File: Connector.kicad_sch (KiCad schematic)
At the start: 3 parts, among them J7 Conn_02x10_Odd_Even

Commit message: Не битый репозиторий
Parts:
- J7: footprint Connector_PinSocket_2.54mm:PinSocket_2x10_P2.54mm_Vertical -> Connector_PinSocket_2.00mm:PinSocket_2x10_P2.00mm_Vertical
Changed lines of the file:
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@@
       (effects (font (size 1.27 1.27)) hide)
     )
-    (property "Footprint" "Connector_PinSocket_2.54mm:PinSocket_2x10_P2.54mm_Vertical" (at 156.21 83.82 0)
+    (property "Footprint" "Connector_PinSocket_2.00mm:PinSocket_2x10_P2.00mm_Vertical" (at 156.21 83.82 0)
       (effects (font (size 1.27 1.27)) hide)
     )

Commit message: Первый вариант
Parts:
- removed J7: Conn_02x10_Odd_Even, Connector_PinSocket_2.00mm:PinSocket_2x10_P2.00mm_Vertical, symbol Connector_Generic:Conn_02x10_Odd_Even
- added J10, J11, J12, J13, J14, J15, J7, J9: Conn_01x02_Pin, Connector_PinHeader_2.54mm:PinHeader_1x02_P2.54mm_Vertical_SMD_Pin1Left, symbol Connector:Conn_01x02_Pin
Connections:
- net +24V: now also J11.1 (Pin_1)
- net A: now also J10.1 (Pin_1)
- net B: now also J7.1 (Pin_1)
- net C: now also J15.2 (Pin_2)
- net G1: now also J10.2 (Pin_2)
- net G2: now also J9.2 (Pin_2)
- net G3: now also J7.2 (Pin_2)
- net G4: now also J13.1 (Pin_1)
- net G5: now also J15.1 (Pin_1)
- net G6: now also J14.1 (Pin_1)
- net GND: now also J11.2 (Pin_2), J13.2 (Pin_2), J14.2 (Pin_2), J9.1 (Pin_1)
- new net Shunt+: J12.2 (Pin_2)
- new net Shunt-: J12.1 (Pin_1)

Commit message: Сохранил схему
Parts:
- added J16: Conn_01x02_Pin, Connector_PinHeader_2.54mm:PinHeader_1x02_P2.54mm_Vertical_SMD_Pin1Left, symbol Connector:Conn_01x02_Pin
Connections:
- new net NTC+: J16.2 (Pin_2)
- new net NTC-: J16.1 (Pin_1)

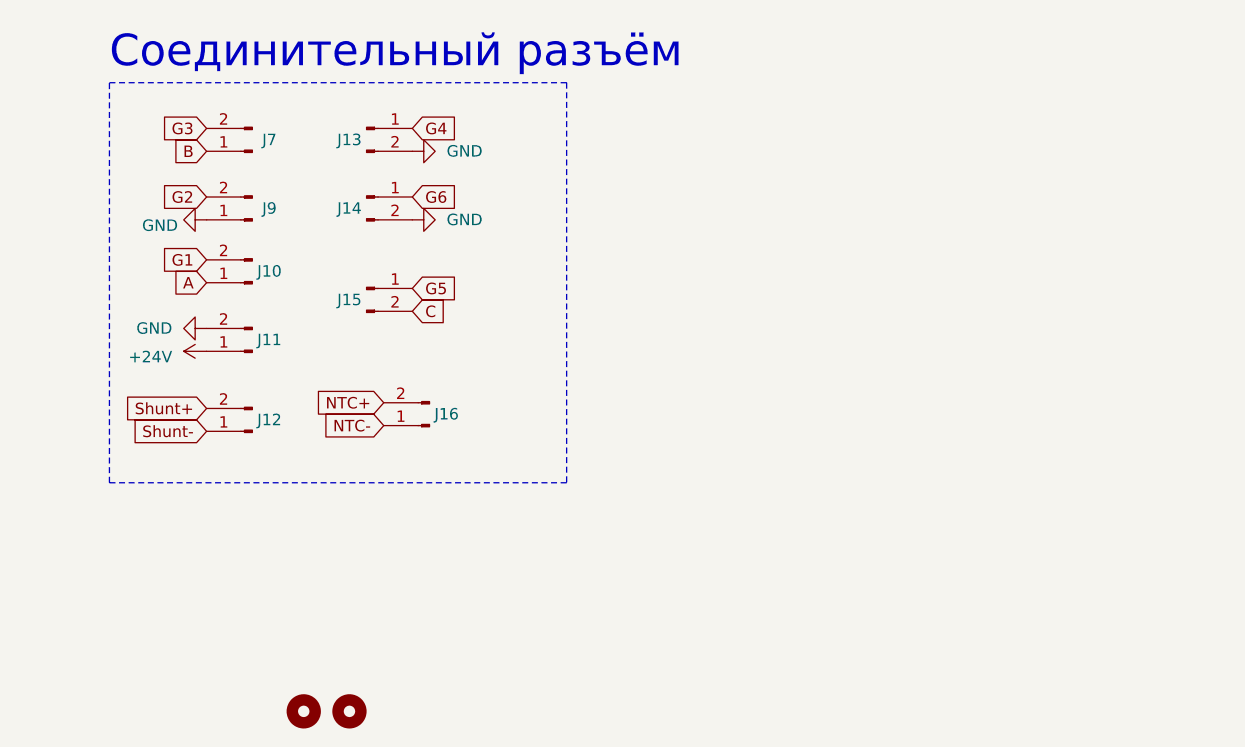
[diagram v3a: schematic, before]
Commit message: Заменил разъёмы 2.54 на 1.27мм
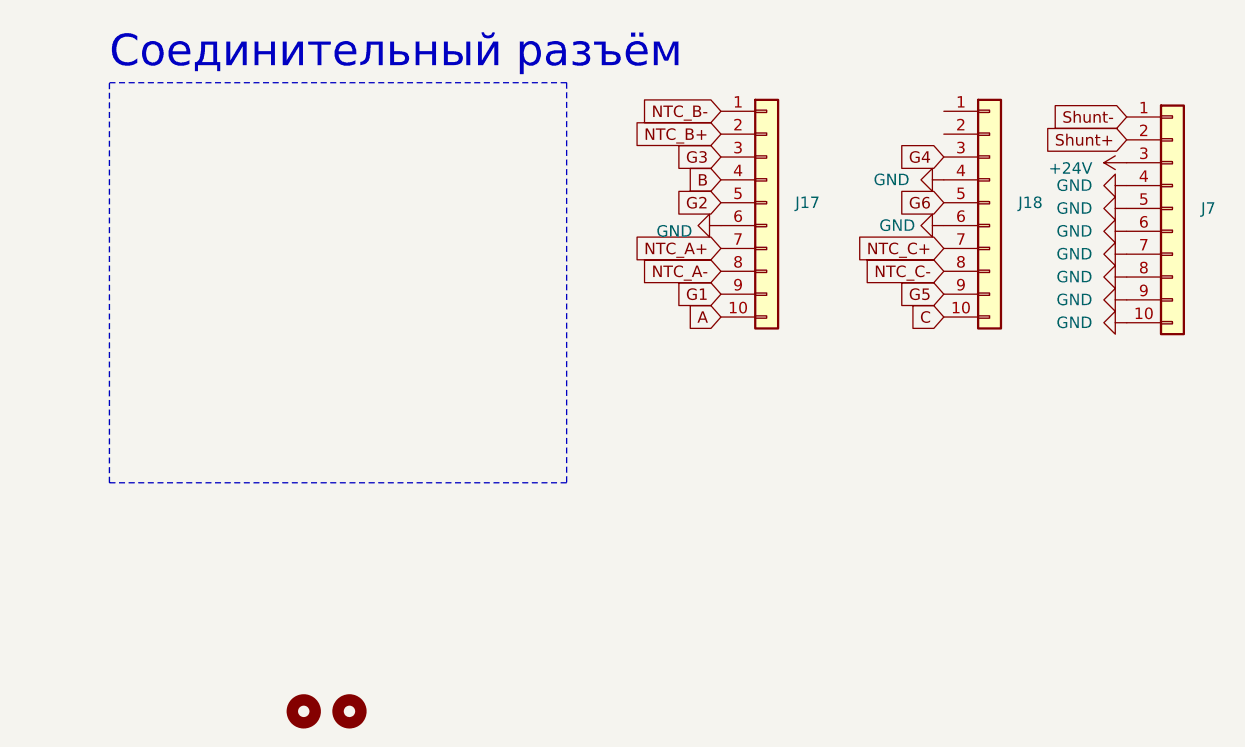
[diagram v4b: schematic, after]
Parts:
- removed J10, J11, J12, J13, J14, J15, J16, J7, J9: Conn_01x02_Pin, Connector_PinHeader_2.54mm:PinHeader_1x02_P2.54mm_Vertical_SMD_Pin1Left, symbol Connector:Conn_01x02_Pin
- added J17, J18, J7: Conn_01x10, Connector_PinSocket_1.27mm:PinSocket_1x10_P1.27mm_Vertical_SMD_Pin1Right, symbol Connector_Generic:Conn_01x10
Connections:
- net +24V: now also J7.3 (Pin_3)
- net A: now also J17.10 (Pin_10)
- net B: now also J17.4 (Pin_4)
- net C: now also J18.10 (Pin_10)
- net G1: now also J17.9 (Pin_9)
- net G2: now also J17.5 (Pin_5)
- net G3: now also J17.3 (Pin_3)
- net G4: now also J18.3 (Pin_3)
- net G5: now also J18.9 (Pin_9)
- net G6: now also J18.5 (Pin_5)
- net GND: now also J17.6 (Pin_6), J18.4 (Pin_4), J18.6 (Pin_6), J7.10 (Pin_10), J7.4 (Pin_4), J7.5 (Pin_5), J7.6 (Pin_6), J7.7 (Pin_7), J7.8 (Pin_8), J7.9 (Pin_9)
- net Shunt+: now also J7.2 (Pin_2)
- net Shunt-: now also J7.1 (Pin_1)
- new net NTC_A+: J17.7 (Pin_7)
- new net NTC_A-: J17.8 (Pin_8)
- new net NTC_B+: J17.2 (Pin_2)
- new net NTC_B-: J17.1 (Pin_1)
- new net NTC_C+: J18.7 (Pin_7)
- new net NTC_C-: J18.8 (Pin_8)

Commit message: Изменения: добавил папку с отчетностью
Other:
- note added: "Соединительные разъёмы"
- note removed: "Соединительный разъём"
- moved on the sheet: J17, J18, J7
